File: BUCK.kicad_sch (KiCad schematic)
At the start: 11 parts, among them U2 TPS562200

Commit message: Updated subsheets
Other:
- moved on the sheet: C3, C4, C5, C6, C7, C8, L1, R1, R2, R3, U2

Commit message: Updated (?) subsheets
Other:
- moved on the sheet: C3, C4, C5, C6, C7, C8, L1, R1, R2, R3, U2

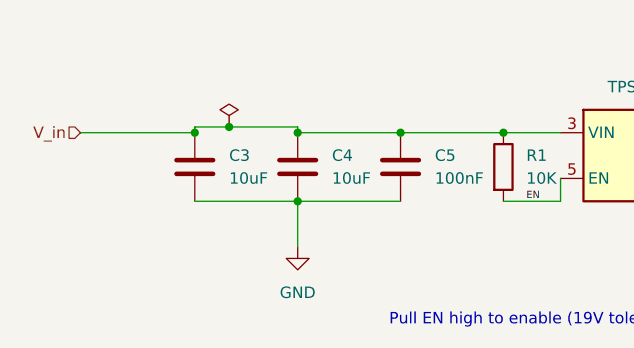
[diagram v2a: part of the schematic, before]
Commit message: Changed connector to 1x6
Will be using Deutsch DT-6
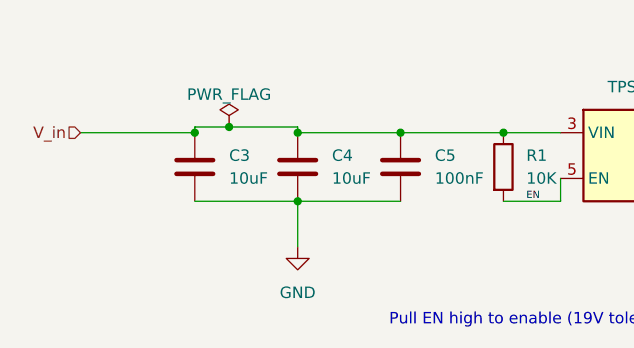
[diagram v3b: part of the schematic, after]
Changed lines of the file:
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@@
       (effects (font (size 1.27 1.27)) hide)
     )
-    (property "Value" "" (id 1) (at 96.52 75.1355 0))
+    (property "Value" "PWR_FLAG" (id 1) (at 96.52 75.1355 0))
     (property "Footprint" "" (id 2) (at 96.52 78.74 0)
       (effects (font (size 1.27 1.27)) hide)

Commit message: Annotated schematic
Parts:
- renumbered C3 to C15, C4 to C16, C5 to C17, C6 to C18, C7 to C19, C8 to C20, R1 to R16, R2 to R17, R3 to R18, U2 to U5
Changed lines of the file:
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@@
   (symbol (lib_id "Device:C") (at 199.39 78.105 0) (unit 1)
     (in_bom yes) (on_board yes) (fields_autoplaced)
-    (property "Reference" "C8" (id 0) (at 203.2 76.8349 0)
+    (property "Reference" "C20" (id 0) (at 203.2 76.8349 0)
       (effects (font (size 1.27 1.27)) (justify left))
     )
@@
   (symbol (lib_id "power:GND") (at 193.04 81.915 0) (unit 1)
     (in_bom yes) (on_board yes) (fields_autoplaced)
-    (property "Reference" "#PWR07" (id 0) (at 193.04 88.265 0)
+    (property "Reference" "#PWR048" (id 0) (at 193.04 88.265 0)
       (effects (font (size 1.27 1.27)) hide)
     )
@@
   (symbol (lib_id "Device:C") (at 185.42 78.105 0) (unit 1)
     (in_bom yes) (on_board yes) (fields_autoplaced)
-    (property "Reference" "C7" (id 0) (at 189.23 76.8349 0)
+    (property "Reference" "C19" (id 0) (at 189.23 76.8349 0)
       (effects (font (size 1.27 1.27)) (justify left))
     )
@@
   (symbol (lib_id "Device:C") (at 92.71 83.185 0) (unit 1)
     (in_bom yes) (on_board yes) (fields_autoplaced)
-    (property "Reference" "C3" (id 0) (at 96.52 81.9149 0)
+    (property "Reference" "C15" (id 0) (at 96.52 81.9149 0)
       (effects (font (size 1.27 1.27)) (justify left))
     )
@@
   (symbol (lib_id "Device:C") (at 104.14 83.185 0) (unit 1)
     (in_bom yes) (on_board yes) (fields_autoplaced)
-    (property "Reference" "C4" (id 0) (at 107.95 81.9149 0)
+    (property "Reference" "C16" (id 0) (at 107.95 81.9149 0)
       (effects (font (size 1.27 1.27)) (justify left))
     )
@@
   (symbol (lib_id "Device:C") (at 115.57 83.185 0) (unit 1)
     (in_bom yes) (on_board yes) (fields_autoplaced)
-    (property "Reference" "C5" (id 0) (at 119.38 81.9149 0)
+    (property "Reference" "C17" (id 0) (at 119.38 81.9149 0)
       (effects (font (size 1.27 1.27)) (justify left))
     )
@@
   (symbol (lib_id "power:GND") (at 143.51 89.535 0) (unit 1)
     (in_bom yes) (on_board yes) (fields_autoplaced)
-    (property "Reference" "#PWR05" (id 0) (at 143.51 95.885 0)
+    (property "Reference" "#PWR046" (id 0) (at 143.51 95.885 0)
       (effects (font (size 1.27 1.27)) hide)
     )
@@
   (symbol (lib_id "Device:R") (at 170.18 84.455 90) (unit 1)
     (in_bom yes) (on_board yes)
-    (property "Reference" "R3" (id 0) (at 170.18 86.995 90))
+    (property "Reference" "R18" (id 0) (at 170.18 86.995 90))
     (property "Value" "54.9K" (id 1) (at 170.18 89.535 90))
     (property "Footprint" "Resistor_SMD:R_0603_1608Metric_Pad0.98x0.95mm_HandSolder" (id 2) (at 170.18 86.233 90)
@@
   (symbol (lib_id "Device:R") (at 127 83.185 0) (unit 1)
     (in_bom yes) (on_board yes) (fields_autoplaced)
-    (property "Reference" "R1" (id 0) (at 129.54 81.9149 0)
+    (property "Reference" "R16" (id 0) (at 129.54 81.9149 0)
       (effects (font (size 1.27 1.27)) (justify left))
     )
@@
   (symbol (lib_id "power:GND") (at 158.75 92.075 0) (unit 1)
     (in_bom yes) (on_board yes) (fields_autoplaced)
-    (property "Reference" "#PWR06" (id 0) (at 158.75 98.425 0)
+    (property "Reference" "#PWR047" (id 0) (at 158.75 98.425 0)
       (effects (font (size 1.27 1.27)) hide)
     )
@@
   (symbol (lib_id "Regulator_Switching:TPS562200") (at 143.51 81.915 0) (unit 1)
     (in_bom yes) (on_board yes) (fields_autoplaced)
-    (property "Reference" "U2" (id 0) (at 143.51 71.755 0))
+    (property "Reference" "U5" (id 0) (at 143.51 71.755 0))
     (property "Value" "TPS562200" (id 1) (at 143.51 74.295 0))
     (property "Footprint" "Package_TO_SOT_SMD:SOT-23-6" (id 2) (at 144.78 88.265 0)
@@
   (symbol (lib_id "Device:C") (at 160.02 78.105 0) (unit 1)
     (in_bom yes) (on_board yes) (fields_autoplaced)
-    (property "Reference" "C6" (id 0) (at 163.83 76.8349 0)
+    (property "Reference" "C18" (id 0) (at 163.83 76.8349 0)
       (effects (font (size 1.27 1.27)) (justify left))
     )
@@
   (symbol (lib_id "Device:R") (at 158.75 88.265 0) (unit 1)
     (in_bom yes) (on_board yes) (fields_autoplaced)
-    (property "Reference" "R2" (id 0) (at 161.29 86.9949 0)
+    (property "Reference" "R17" (id 0) (at 161.29 86.9949 0)
       (effects (font (size 1.27 1.27)) (justify left))
     )
@@
   (symbol (lib_id "power:PWR_FLAG") (at 96.52 78.74 0) (unit 1)
     (in_bom yes) (on_board yes) (fields_autoplaced)
-    (property "Reference" "#FLG03" (id 0) (at 96.52 76.835 0)
+    (property "Reference" "#FLG02" (id 0) (at 96.52 76.835 0)
       (effects (font (size 1.27 1.27)) hide)
     )
@@
   (symbol (lib_id "power:GND") (at 104.14 92.075 0) (unit 1)
     (in_bom yes) (on_board yes) (fields_autoplaced)
-    (property "Reference" "#PWR04" (id 0) (at 104.14 98.425 0)
-      (effects (font (size 1.27 1.27)) hide)
-    )
+    (property "Reference" "#PWR045" (id 0) (at 104.14 98.425 0)
+      (effects (font (size 1.27 1.27)) hide)
+    )
